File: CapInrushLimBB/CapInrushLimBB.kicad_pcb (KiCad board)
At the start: 2 copper layers, 100 x 74.5 mm, 28 parts, among them J2 Screw_Terminal_01x02, J3 Screw_Terminal_01x02, K1 G5LE-1, Q1 IRF9540N, Q2 Q_PMOS_GDSD, Q3 MPSA42, Q4 MPSA42

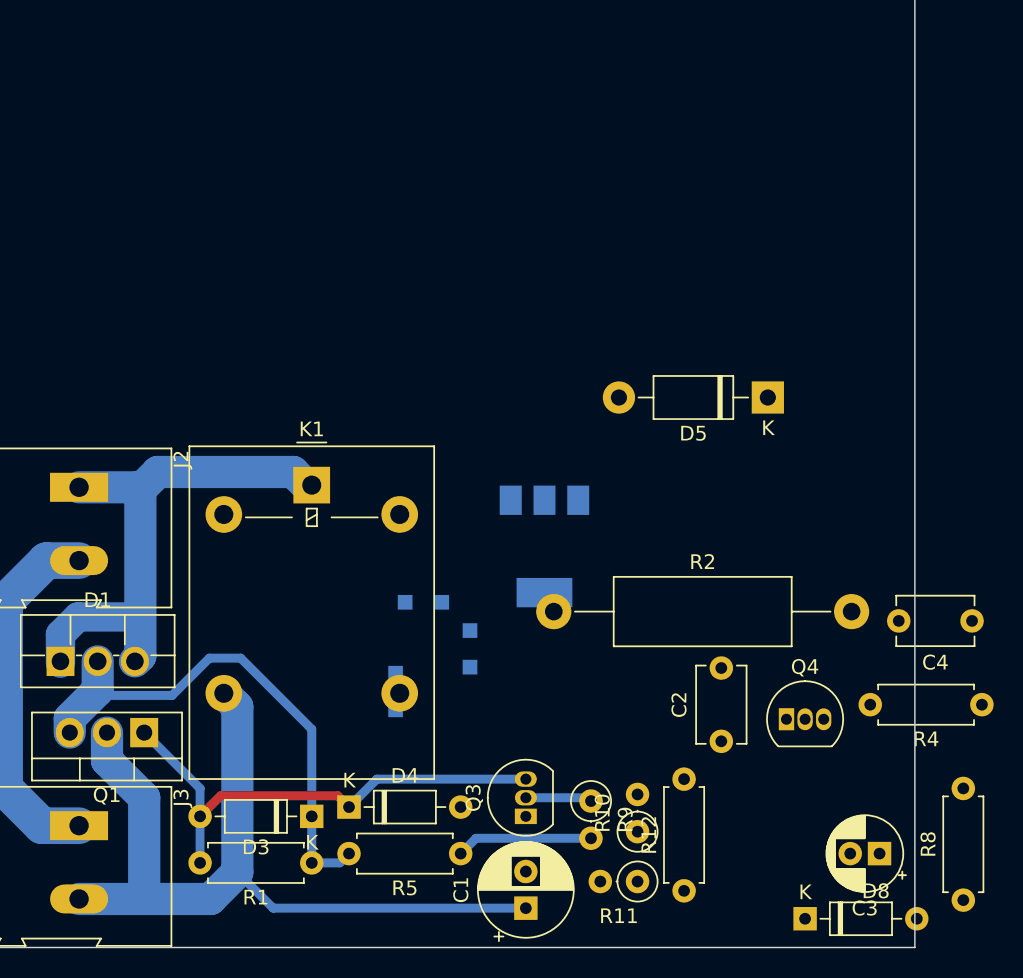
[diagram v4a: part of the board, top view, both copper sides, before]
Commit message: Updated values and footprints.
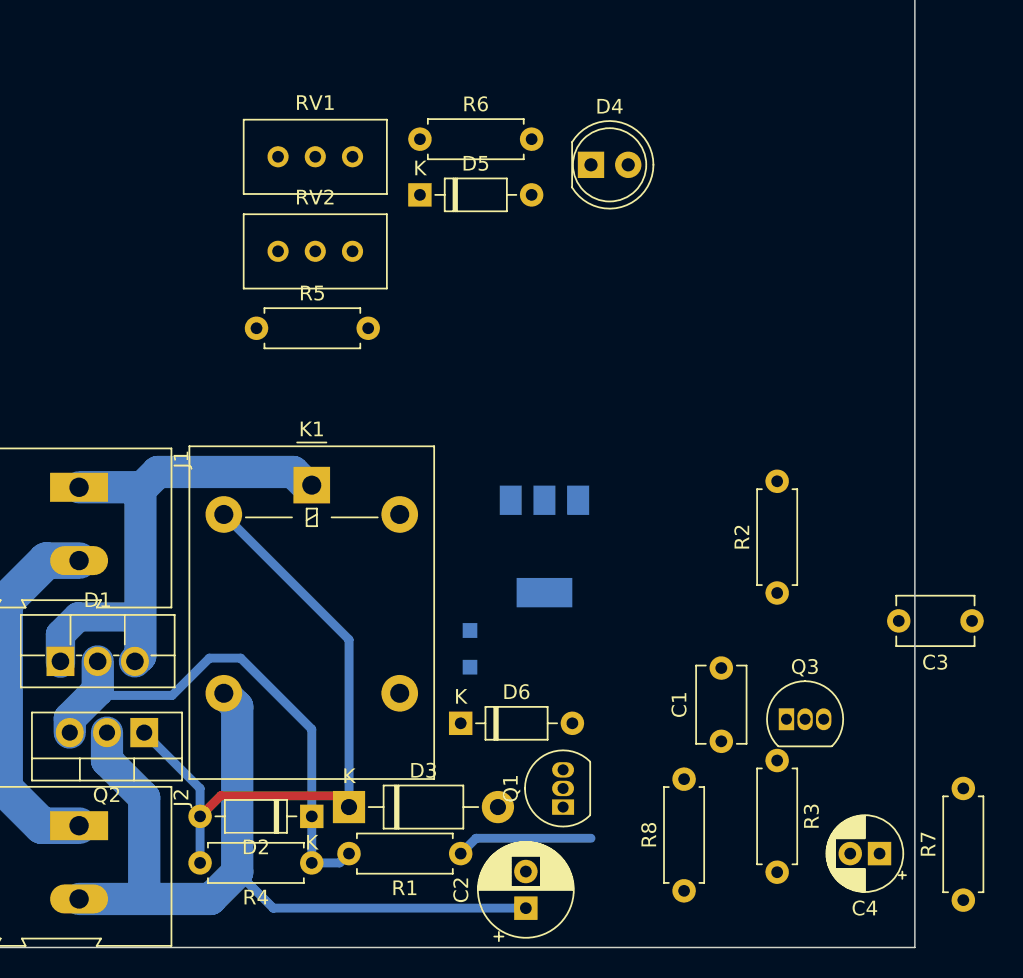
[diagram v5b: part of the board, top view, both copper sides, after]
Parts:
- removed the D6 at (242.6, 142.6)
- removed the D7 at (244.5, 136.5)
- removed D8: BZX55C5V6, Diode_THT:D_DO-35_SOD27_P7.62mm_Horizontal
- removed R11: 1k, Resistor_THT:R_Axial_DIN0207_L6.3mm_D2.5mm_P2.54mm_Vertical
- removed the R2 at (253.4, 137.2)
- removed the R4 at (282.6, 143.5)
- added D4: Red LED, LED_THT:LED_D5.0mm, F.Cu at (255.9, 106.7)
- added D5: BZY88-C9V1, Diode_THT:D_DO-35_SOD27_P7.62mm_Horizontal, F.Cu at (244.2, 108.7)
- added R5: 1k, Resistor_THT:R_Axial_DIN0207_L6.3mm_D2.5mm_P7.62mm_Horizontal, F.Cu at (233.1, 117.8)
- added R6: 100R, Resistor_THT:R_Axial_DIN0207_L6.3mm_D2.5mm_P7.62mm_Horizontal, F.Cu at (244.2, 104.9)
- added RV1: 10k, Potentiometer_THT:Potentiometer_Bourns_3296W_Vertical, F.Cu at (239.6, 106.1)
- added RV2: 1k, Potentiometer_THT:Potentiometer_Bourns_3296W_Vertical, F.Cu at (239.6, 112.6)
- D2: renamed from D3; value BZX79-C15 -> BZY88-C9V1
- R2: renamed from R10; footprint Resistor_THT:R_Axial_DIN0207_L6.3mm_D2.5mm_P2.54mm_Vertical -> Resistor_THT:R_Axial_DIN0207_L6.3mm_D2.5mm_P7.62mm_Horizontal
- R3: renamed from R9; footprint Resistor_THT:R_Axial_DIN0207_L6.3mm_D2.5mm_P2.54mm_Vertical -> Resistor_THT:R_Axial_DIN0207_L6.3mm_D2.5mm_P7.62mm_Horizontal
- R8: renamed from R12; value 100k -> 200k
- moved D3 40.0 mm to (239.4, 150.5), turned to 0 degrees
- moved R2 18.9 mm to (268.6, 135.9)
- moved R3 13.0 mm to (268.6, 147.3)
- moved D6 9.52 mm to (247.0, 144.8)
- moved Q1 2.62 mm to (254.0, 150.5)
- renumbered C2 to C1, C1 to C2, C4 to C3, C3 to C4, D5 to D3, D4 to D6, D2 to D7, J2 to J1, J3 to J2, Q3 to Q1, Q1 to Q2, Q4 to Q3, Q2 to Q4, R5 to R1, R1 to R4, R8 to R7
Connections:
- C3 pad 1: Net-(C4-Pad1) -> /Gnd
- C3 pad 2: /Gnd -> Net-(C3-Pad2)
- C4 pad 1: Net-(C3-Pad1) -> Net-(C4-Pad1)
- D2 pad 2: Net-(D3-Pad2) -> /RLCoilHigh
- D3 pad 1: Net-(D5-Pad1) -> /RLCoilHigh
- D3 pad 2: Net-(D5-Pad2) -> /RLCoilLow
- D6 pad 1: Net-(D3-Pad2) -> Net-(C4-Pad1)
- D6 pad 2: Net-(D2-Pad1) -> Net-(C3-Pad2)
- D7 pad 1: Net-(D2-Pad1) -> Net-(D5-Pad1)
- K1 pad 2: Net-(D5-Pad2) -> /RLCoilHigh
- K1 pad 5: Net-(K1-Pad5) -> /RLCoilLow
- Q1 pad 3: Net-(D3-Pad2) -> /RLCoilHigh
- Q2 pad 1: Net-(D3-Pad2) -> /RLCoilHigh
- Q3 pad 1: /Gnd -> Net-(Q3-Pad1)
- Q3 pad 2: Net-(C4-Pad1) -> Net-(C3-Pad2)
- Q3 pad 3: Net-(D6-Pad1) -> /RLCoilLow
- Q4 pad 1: Net-(D3-Pad2) -> /RLCoilHigh
- Q4 pad 2: Net-(D5-Pad1) -> Net-(Q4-Pad2)
- Q4 pad 3: Net-(D2-Pad1) -> Net-(D5-Pad1)
- Q4 pad 4: Net-(D5-Pad1) -> Net-(Q4-Pad2)
- R4 pad 2: Net-(D3-Pad2) -> /RLCoilHigh
- R7 pad 1: Net-(C3-Pad1) -> Net-(C4-Pad1)
- R7 pad 2: Net-(D5-Pad1) -> Net-(Q4-Pad2)
- R8 pad 2: Net-(C3-Pad1) -> Net-(C4-Pad1)
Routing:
- net /RLCoilHigh: track 0.00 -> 43.9 mm
- net Net-(D3-Pad2): track 34.4 -> 0.00 mm
- net Net-(C1-Pad1): track 4.54 -> 0.00 mm

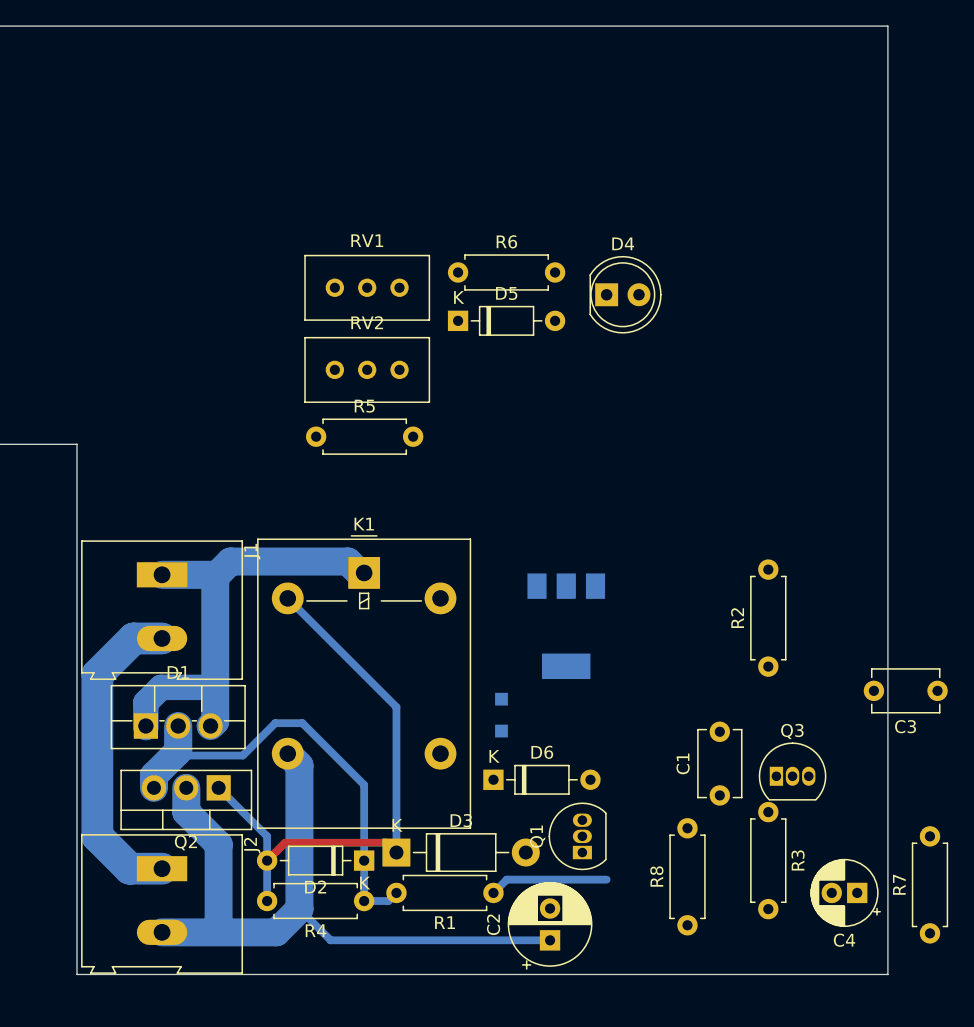
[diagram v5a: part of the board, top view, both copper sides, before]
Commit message: First layout complete
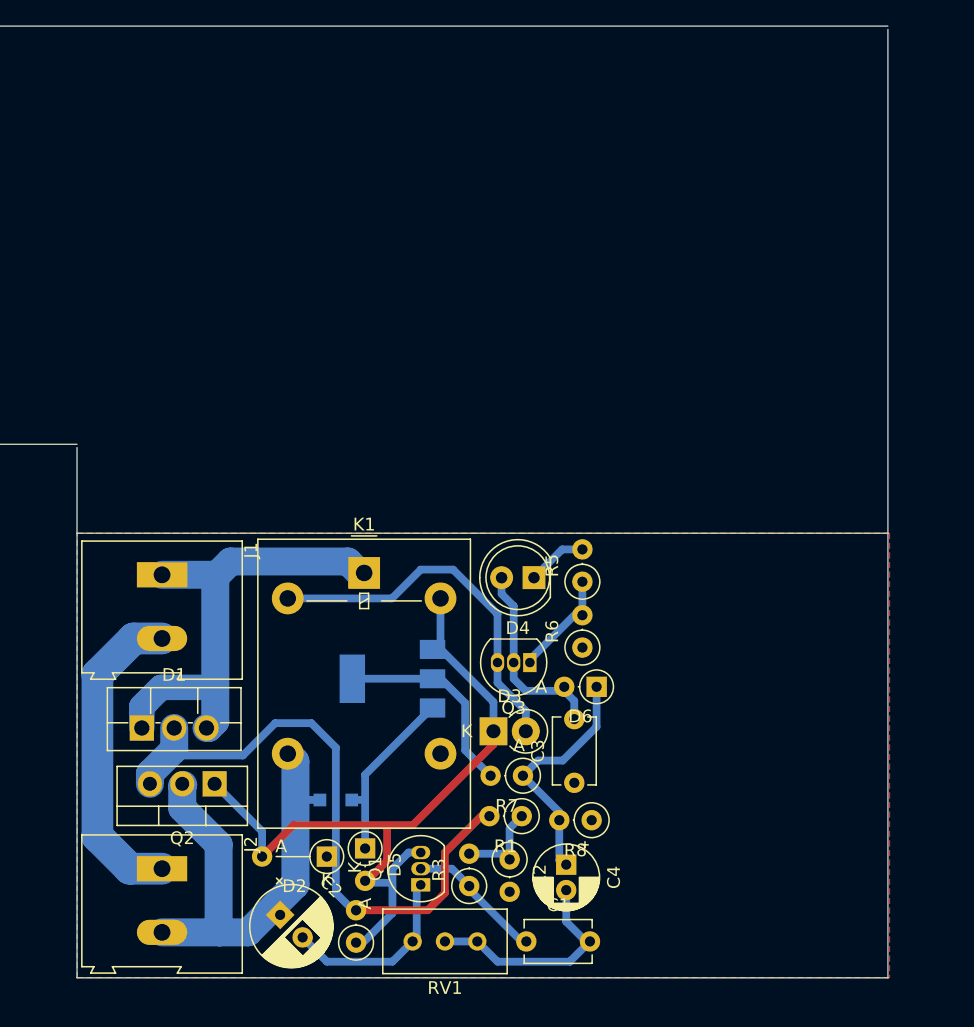
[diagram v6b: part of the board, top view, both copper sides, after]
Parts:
- removed RV2: 1k, Potentiometer_THT:Potentiometer_Bourns_3296W_Vertical
- D2: footprint Diode_THT:D_DO-35_SOD27_P7.62mm_Horizontal -> Diode_THT:D_DO-35_SOD27_P5.08mm_Vertical_AnodeUp
- D3: footprint Diode_THT:D_DO-41_SOD81_P10.16mm_Horizontal -> Diode_THT:D_DO-41_SOD81_P2.54mm_Vertical_KathodeUp
- D5, D6: footprint Diode_THT:D_DO-35_SOD27_P7.62mm_Horizontal -> Diode_THT:D_DO-35_SOD27_P2.54mm_Vertical_AnodeUp
- R1, R2, R3, R4, R6, R7, R8: footprint Resistor_THT:R_Axial_DIN0207_L6.3mm_D2.5mm_P7.62mm_Horizontal -> Resistor_THT:R_Axial_DIN0207_L6.3mm_D2.5mm_P2.54mm_Vertical
- R5: value 1k -> 1k5; footprint Resistor_THT:R_Axial_DIN0207_L6.3mm_D2.5mm_P7.62mm_Horizontal -> Resistor_THT:R_Axial_DIN0207_L6.3mm_D2.5mm_P2.54mm_Vertical
- moved RV1 51.4 mm to (240.7, 157.5), turned to 180 degrees
- moved D5 42.1 mm to (236.9, 150.2), turned to -90 degrees
- moved R7 34.3 mm to (249.3, 144.5), turned to 180 degrees
- moved R6 31.0 mm to (254.0, 134.4), turned to 90 degrees
- moved C3 29.4 mm to (253.4, 145.0), turned to 90 degrees
- moved R2 25.3 mm to (248.3, 151.0), turned to -90 degrees
- moved R3 24.2 mm to (245.1, 153.1), turned to 90 degrees
- moved R5 23.8 mm to (254.0, 129.2), turned to 90 degrees
- moved C4 23.0 mm to (252.7, 151.4), turned to -90 degrees
- moved D4 22.9 mm to (250.2, 128.9), turned to 180 degrees
- moved Q3 21.3 mm to (249.9, 135.6), turned to 180 degrees
- moved C2 21.3 mm to (230.3, 155.4), turned to -45 degrees
- moved C1 19.0 mm to (249.6, 157.5), turned to 0 degrees
- moved D7 14.6 mm to (234.6, 146.4), turned to 180 degrees
- moved Q4 14.3 mm to (239.1, 136.8), turned to 180 degrees
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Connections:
- K1 pad 2: /RLCoilHigh -> /RLCoilLow
- K1 pad 5: /RLCoilLow -> /RLCoilHigh
- R2 pad 1: /Gnd -> Net-(R1-Pad1)
- R2 pad 2: Net-(R1-Pad1) -> /Gnd
- R4 pad 1: /PolProtect -> /RLCoilHigh
- R4 pad 2: /RLCoilHigh -> /PolProtect
- R5 pad 2: Net-(R5-Pad2) -> /Gnd
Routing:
- net /RLCoilLow: track 0.00 -> 29.0 mm
- net /Gnd: track 25.1 -> 47.1 mm
- net /RL_Output: track 56.7 -> 37.5 mm
- net Net-(C4-Pad1): track 0.00 -> 18.8 mm
- net /RLCoilHigh: track 43.9 -> 60.5 mm
- net Net-(Q4-Pad2): track 0.00 -> 16.2 mm
- net Net-(C3-Pad2): track 0.00 -> 15.6 mm
- net Net-(C2-Pad2): track 0.00 -> 15.0 mm
- net Net-(D5-Pad1): track 0.00 -> 14.5 mm
- net /PolProtect: track 35.4 -> 48.2 mm
- net Net-(C1-Pad1): track 0.00 -> 10.8 mm
- net Net-(Q3-Pad1): track 0.00 -> 8.06 mm
- net Net-(R1-Pad1): track 9.32 -> 6.88 mm
- net /RL_Input: track 36.6 -> 37.1 mm
- added copper zone on F.Cu, net /Gnd
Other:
- board size 100 x 74.5 mm -> 100 x 74.8 mm

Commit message: Tweaked board outline.
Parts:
- moved C3 0.32 mm to (253.7, 145.0)
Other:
- board size 100 x 74.8 mm -> 42.2 x 34.9 mm
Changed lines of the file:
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@@
   )
   (footprint "Capacitor_THT:C_Disc_D5.1mm_W3.2mm_P5.00mm" (layer "F.Cu")
-    (at 253.365 145.0175 90)
+    (at 253.6825 145.0175 90)
     (descr "C, Disc series, Radial, pin pitch=5.00mm, , diameter*width=5.1*3.2mm^2, Capacitor, http://www.vishay.com/docs/45233/krseries.pdf")
     (tags "C Disc series Radial pin pitch 5.00mm  diameter 5.1mm width 3.2mm Capacitor")
@@
     )
   )
-  (gr_line locked (start 178 85.575) (end 278 85.575) (layer "Edge.Cuts") (width 0.1))
-  (gr_line locked (start 214.3 118.6875) (end 214.3 160.3375) (layer "Edge.Cuts") (width 0.1))
-  (gr_line (start 214.3 125.41125) (end 278 125.41375) (layer "Edge.Cuts") (width 0.1))
-  (gr_line locked (start 278 160.3375) (end 214.3 160.3375) (layer "Edge.Cuts") (width 0.1))
-  (gr_line locked (start 178 118.425) (end 178 85.575) (layer "Edge.Cuts") (width 0.1))
-  (gr_line locked (start 278 85.8375) (end 278 160.3375) (layer "Edge.Cuts") (width 0.1))
-  (gr_line locked (start 178 118.425) (end 214.3 118.425) (layer "Edge.Cuts") (width 0.1))
+  (gr_line (start 214.3125 125.41) (end 256.54 125.4125) (layer "Edge.Cuts") (width 0.1))
+  (gr_line (start 256.54 125.4125) (end 256.54 160.3375) (layer "Edge.Cuts") (width 0.1))
+  (gr_line (start 214.3125 160.3375) (end 214.3125 125.41) (layer "Edge.Cuts") (width 0.1))
+  (gr_line locked (start 256.54 160.3375) (end 214.3125 160.3375) (layer "Edge.Cuts") (width 0.1))
   (segment (start 225.425 149.86) (end 225.425 156.685) (width 2.2) (layer "B.Cu") (net 1))
   (segment (start 222.648048 145.178048) (end 222.5675 145.258596) (width 2.2) (layer "B.Cu") (net 1))
@@
   (segment (start 255.114315 140.611682) (end 255.114315 137.795) (width 0.6096) (layer "B.Cu") (net 4))
   (segment (start 250.521811 143.270689) (end 252.455308 143.270689) (width 0.6096) (layer "B.Cu") (net 4))
+  (segment (start 252.4125 147.955) (end 252.4125 151.025689) (width 0.6096) (layer "B.Cu") (net 4))
   (segment (start 252.455308 143.270689) (end 255.114315 140.611682) (width 0.6096) (layer "B.Cu") (net 4))
   (segment (start 249.33 144.4625) (end 250.521811 143.270689) (width 0.6096) (layer "B.Cu") (net 4))
-  (segment (start 252.1875 151.115577) (end 252.73 151.658077) (width 0.6096) (layer "B.Cu") (net 4))
+  (segment (start 252.4125 151.025689) (end 252.73 151.343189) (width 0.6096) (layer "B.Cu") (net 4))
   (segment (start 252.1875 148.2725) (end 252.1875 147.32) (width 0.6096) (layer "B.Cu") (net 4))
-  (segment (start 252.1875 148.2725) (end 252.1875 151.115577) (width 0.6096) (layer "B.Cu") (net 4))
+  (segment (start 252.1875 147.955) (end 252.4125 147.955) (width 0.6096) (layer "B.Cu") (net 4))
   (segment (start 252.1875 147.32) (end 249.33 144.4625) (width 0.6096) (layer "B.Cu") (net 4))
   (segment (start 219.3925 139.035) (end 219.3925 140.7125) (width 2) (layer "B.Cu") (net 5))
@@
   (segment (start 224.633 140.7125) (end 225.16 140.1855) (width 2.2) (layer "B.Cu") (net 5))
   (segment (start 236.4825 128.5325) (end 235.585 127.635) (width 2.2) (layer "B.Cu") (net 5))
-  (segment (start 249.555 137.795) (end 248.6025 136.8425) (width 0.6096) (layer "B.Cu") (net 6))
-  (segment (start 248.6025 136.8425) (end 248.6025 135.5725) (width 0.6096) (layer "B.Cu") (net 6))
+  (segment (start 248.6025 136.8425) (end 249.555 137.795) (width 0.6096) (layer "B.Cu") (net 6))
   (segment (start 247.655 128.905) (end 247.655 130.18) (width 0.6096) (layer "B.Cu") (net 6))
-  (segment (start 252.574315 137.795) (end 249.555 137.795) (width 0.6096) (layer "B.Cu") (net 6))
-  (segment (start 253.365 138.585685) (end 252.574315 137.795) (width 0.6096) (layer "B.Cu") (net 6))
+  (segment (start 252.574315 137.795) (end 253.6825 138.903185) (width 0.6096) (layer "B.Cu") (net 6))
   (segment (start 247.655 130.18) (end 248.6025 131.1275) (width 0.6096) (layer "B.Cu") (net 6))
-  (segment (start 253.365 140.375) (end 253.365 138.585685) (width 0.6096) (layer "B.Cu") (net 6))
+  (segment (start 248.6025 135.5725) (end 248.6025 136.8425) (width 0.6096) (layer "B.Cu") (net 6))
+  (segment (start 253.6825 138.903185) (end 253.6825 140.0175) (width 0.6096) (layer "B.Cu") (net 6))
+  (segment (start 249.555 137.795) (end 252.574315 137.795) (width 0.6096) (layer "B.Cu") (net 6))
   (segment (start 248.6025 131.1275) (end 248.6025 135.5725) (width 0.6096) (layer "B.Cu") (net 6))
   (segment (start 247.015 142.000342) (end 247.015 140.97) (width 0.6096) (layer "F.Cu") (net 7))
@@
     (polygon
       (pts
-        (xy 278.13 160.3375)
+        (xy 256.54 160.3375)
         (xy 214.3125 160.3375)
         (xy 214.3125 125.4125)
-        (xy 278.13 125.4125)
+        (xy 256.54 125.4125)
       )
     )

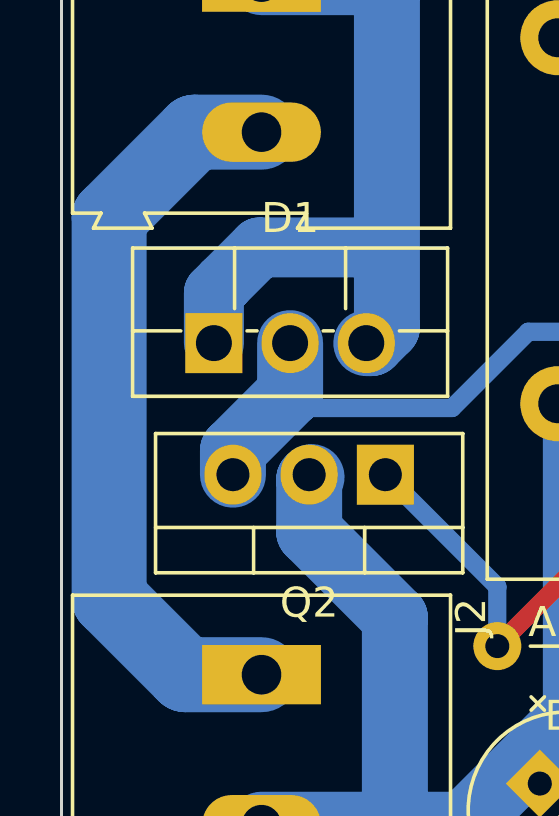
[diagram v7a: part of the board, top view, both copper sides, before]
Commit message: Added via linking top pour to Gnd.
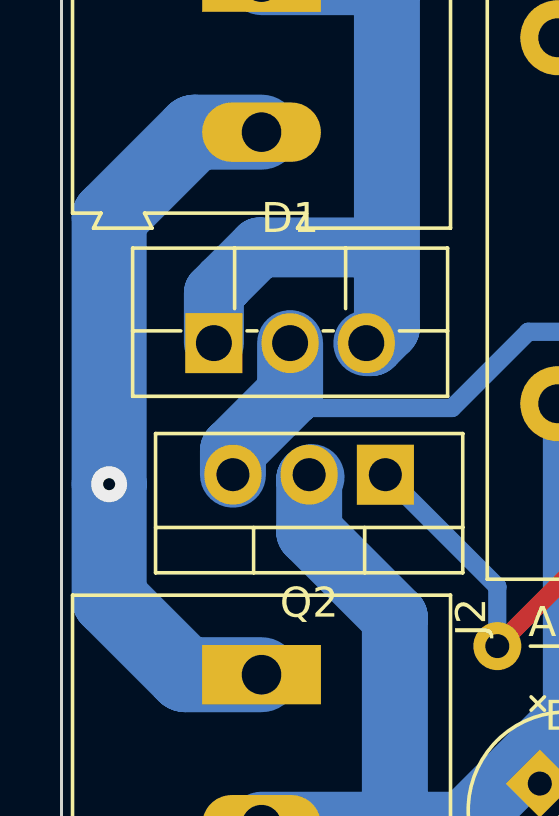
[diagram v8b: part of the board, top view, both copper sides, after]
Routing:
- net /Gnd: vias 0 -> 1
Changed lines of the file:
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@@
   (segment (start 249.2375 147.6375) (end 248.285 148.59) (width 0.6096) (layer "B.Cu") (net 12))
   (segment (start 248.285 148.59) (end 248.285 151.0375) (width 0.6096) (layer "B.Cu") (net 12))
+  (via (at 215.9 145.415) (size 1.2) (drill 0.4) (layers "F.Cu" "B.Cu") (net 13))
   (segment (start 215.9 136.525) (end 218.745 133.68) (width 2.5) (layer "B.Cu") (net 13))
   (segment (start 252.4175 126.6825) (end 250.195 128.905) (width 0.6096) (layer "B.Cu") (net 13))
-  (segment (start 215.9 149.225) (end 215.9 136.525) (width 2.5) (layer "B.Cu") (net 13))
+  (segment (start 215.9 149.225) (end 215.9 145.415) (width 2.5) (layer "B.Cu") (net 13))
   (segment (start 220.98 151.765) (end 218.44 151.765) (width 2.5) (layer "B.Cu") (net 13))
   (segment (start 254 126.6825) (end 252.4175 126.6825) (width 0.6096) (layer "B.Cu") (net 13))
+  (segment (start 215.9 145.415) (end 215.9 136.525) (width 2.5) (layer "B.Cu") (net 13))
   (segment (start 252.73 153.866699) (end 252.73 155.9325) (width 0.6096) (layer "B.Cu") (net 13))
   (segment (start 253.0275 159.0675) (end 247.3525 159.0675) (width 0.6096) (layer "B.Cu") (net 13))
